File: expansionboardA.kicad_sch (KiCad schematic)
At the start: 62 parts, among them J1 DEBUG, J2 USB_A_Stacked, J3 HDMI_A, J4 FAN, P1 USB_C_Plug, U1 MAX3420EECJ, U2 GPIO_U2, U3 AMS1117-3.3, U4 GPIO_U4, U5 MCP3008T-I/SL, U6 CS4344-CZZR, U7 MAX3421EEHJ+T, Y1 Crystal, Y2 Crystal

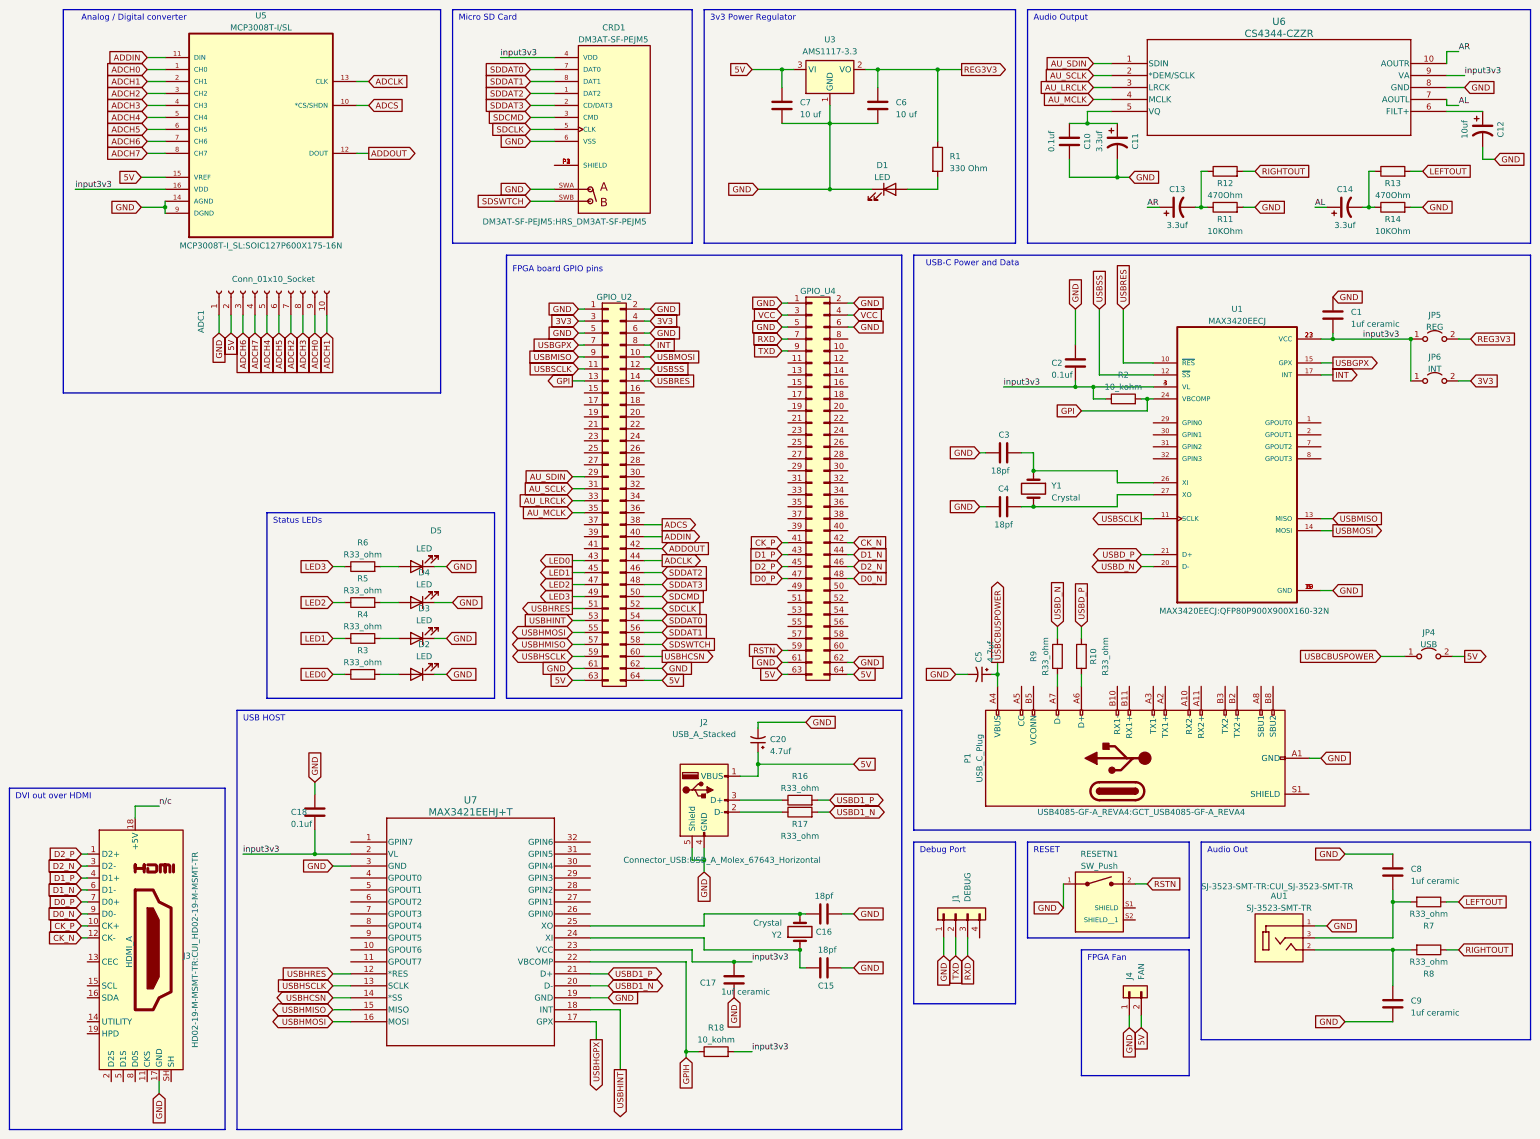
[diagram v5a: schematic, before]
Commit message: Cleaned up board layout
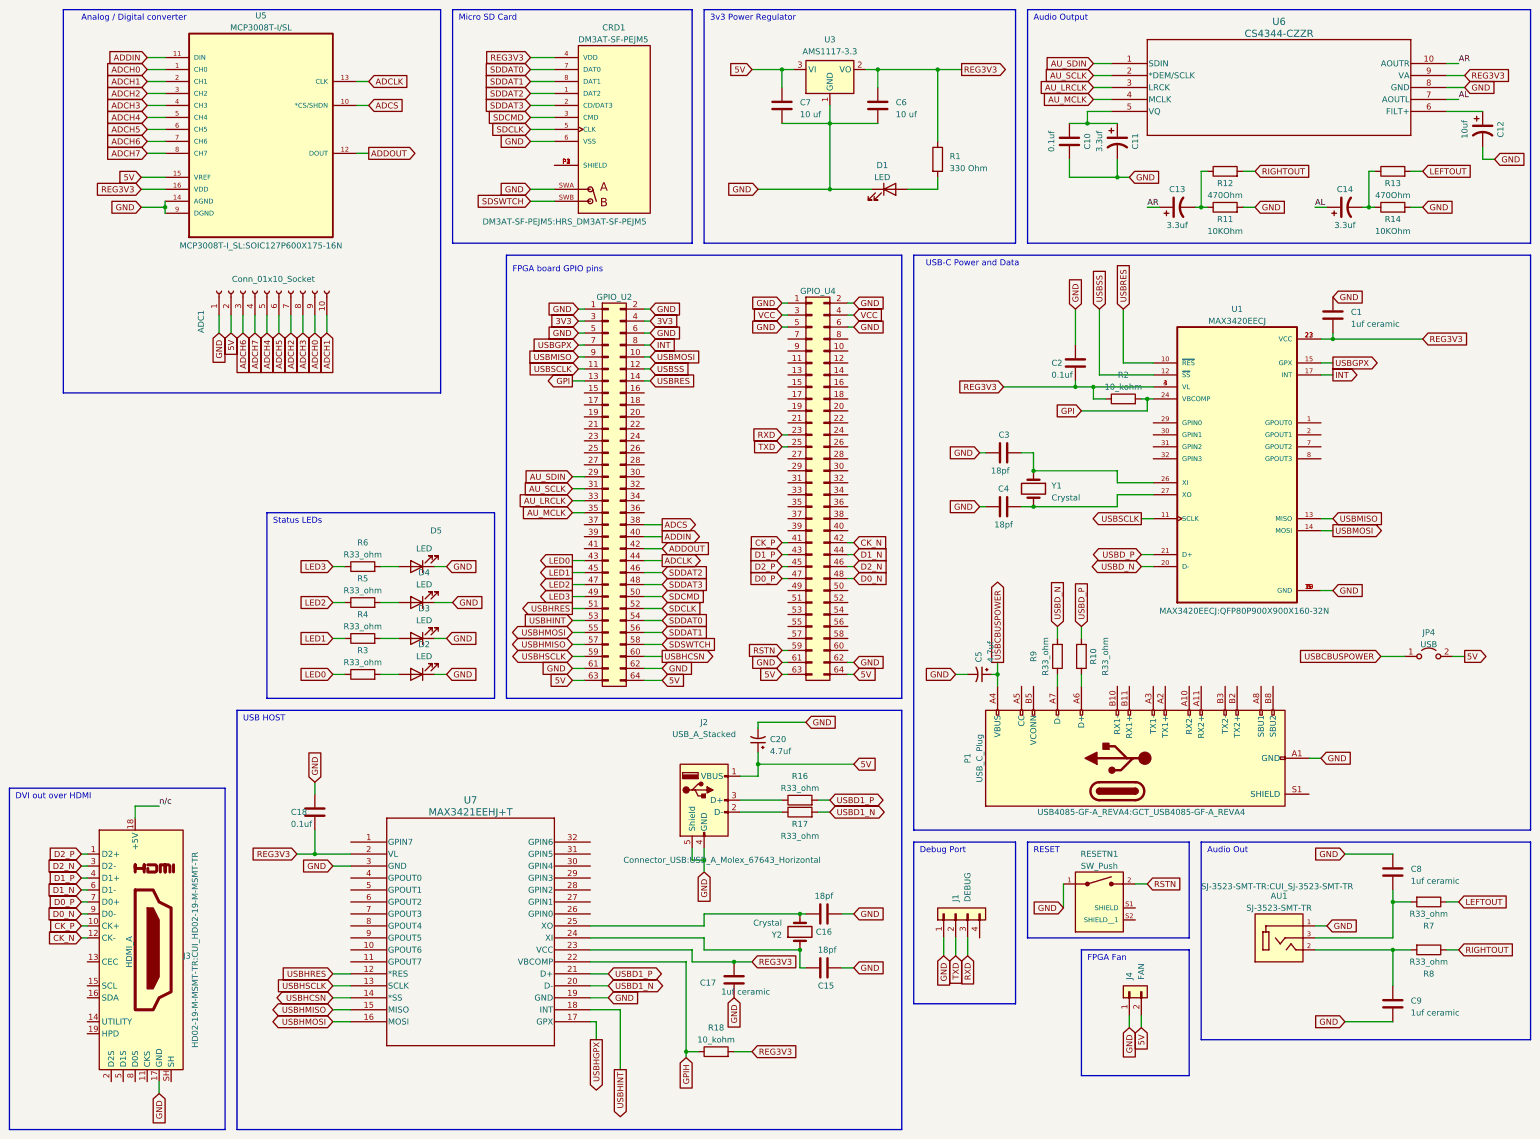
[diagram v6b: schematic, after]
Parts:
- removed JP5: REG, Jumper:SolderJumper-2_P1.3mm_Open_Pad1.0x1.5mm, symbol Jumper:Jumper_2_Open
- removed JP6: INT, Jumper:SolderJumper-2_P1.3mm_Open_Pad1.0x1.5mm, symbol Jumper:Jumper_2_Open
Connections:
- net input3v3 is gone; now on net REG3V3: C1.2, C17.2, C18.2, C2.2, CRD1.4 (VDD), R18.2, R2.1, U1.22 (VCC), U1.23 (VCC), U1.3 (VL), U1.4 (VL), U5.16 (VDD), U6.9 (VA), U7.2 (VL), U7.23 (VCC)
- net RXD: now also U4.23 (Pin_23); no longer U4.7 (Pin_7)
- net TXD: now also U4.25 (Pin_25); no longer U4.9 (Pin_9)

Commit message: Updat4ed some routing
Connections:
- net pin_removed: now reaches U4.7 (Pin_7)
- net pin_removed: now also U4.8 (Pin_8)
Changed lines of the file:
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@@
+    (stroke (width 0) (type default))
+  )
+  (wire (pts (xy 259.08 85.09) (xy 260.35 85.09))
     (stroke (width 0) (type default))
   )
@@
     (stroke (width 0) (type default))
   )
+  (wire (pts (xy 233.68 85.09) (xy 246.38 85.09))
+    (stroke (width 0) (type default))
+  )
   (wire (pts (xy 255.27 39.37) (xy 255.27 53.34))
     (stroke (width 0) (type default))
@@
     (effects (font (size 1.27 1.27)) (justify left bottom))
   )
+  (label "pin_removed" (at 233.68 85.09 0) (fields_autoplaced)
+    (effects (font (size 1.27 1.27)) (justify left bottom))
+  )
   (label "AR" (at 388.62 26.67 0) (fields_autoplaced)
     (effects (font (size 1.27 1.27)) (justify left bottom))
@@
     (effects (font (size 1.27 1.27)) (justify left bottom))
   )
+  (label "pin_removed" (at 260.35 85.09 0) (fields_autoplaced)
+    (effects (font (size 1.27 1.27)) (justify left bottom))
+  )

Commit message: Board changes
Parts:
- C20, C5: footprint Capacitor_THT:CP_Radial_D4.0mm_P1.50mm -> Capacitor_SMD:CP_Elec_4x5.4
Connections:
- net SDCMD: now also U2.54 (Pin_54); no longer U2.50 (Pin_50)
- net SDDAT0: now also U2.50 (Pin_50); no longer U2.54 (Pin_54)
- net SDDAT1: now also U2.48 (Pin_48); no longer U2.56 (Pin_56)
- net SDDAT2: now also U2.58 (Pin_58); no longer U2.46 (Pin_46)
- net SDDAT3: now also U2.56 (Pin_56); no longer U2.48 (Pin_48)
- net SDSWTCH: now also U2.46 (Pin_46); no longer U2.58 (Pin_58)
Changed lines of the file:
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@@
     (stroke (width 0) (type default))
   )
-  (wire (pts (xy 219.71 139.7) (xy 215.9 139.7))
-    (stroke (width 0) (type default))
-  )
   (wire (pts (xy 200.66 152.4) (xy 203.2 152.4))
     (stroke (width 0) (type default))
@@
     (stroke (width 0) (type default))
   )
+  (wire (pts (xy 215.9 147.32) (xy 219.71 147.32))
+    (stroke (width 0) (type default))
+  )
   (wire (pts (xy 219.71 132.08) (xy 215.9 132.08))
     (stroke (width 0) (type default))
@@
     (stroke (width 0) (type default))
   )
-  (wire (pts (xy 219.71 134.62) (xy 215.9 134.62))
-    (stroke (width 0) (type default))
-  )
   (wire (pts (xy 358.14 214.63) (xy 374.65 214.63))
     (stroke (width 0) (type default))
@@
     (stroke (width 0) (type default))
   )
-  (wire (pts (xy 219.71 144.78) (xy 215.9 144.78))
-    (stroke (width 0) (type default))
-  )
   (wire (pts (xy 388.62 214.63) (xy 386.08 214.63))
     (stroke (width 0) (type default))
@@
     (stroke (width 0) (type default))
   )
-  (wire (pts (xy 361.95 83.82) (xy 361.95 85.09))
+  (wire (pts (xy 215.9 134.62) (xy 219.71 134.62))
     (stroke (width 0) (type default))
   )
-  (wire (pts (xy 219.71 142.24) (xy 215.9 142.24))
+  (wire (pts (xy 361.95 83.82) (xy 361.95 85.09))
     (stroke (width 0) (type default))
   )
@@
     (stroke (width 0) (type default))
   )
-  (wire (pts (xy 278.13 53.34) (xy 278.13 50.8))
+  (wire (pts (xy 215.9 149.86) (xy 219.71 149.86))
     (stroke (width 0) (type default))
   )
-  (wire (pts (xy 245.11 39.37) (xy 255.27 39.37))
+  (wire (pts (xy 278.13 53.34) (xy 278.13 50.8))
     (stroke (width 0) (type default))
   )
-  (wire (pts (xy 219.71 137.16) (xy 215.9 137.16))
+  (wire (pts (xy 245.11 39.37) (xy 255.27 39.37))
     (stroke (width 0) (type default))
   )
@@
     (stroke (width 0) (type default))
   )
+  (wire (pts (xy 215.9 142.24) (xy 219.71 142.24))
+    (stroke (width 0) (type default))
+  )
   (wire (pts (xy 217.17 88.9) (xy 215.9 88.9))
     (stroke (width 0) (type default))
@@
     (stroke (width 0) (type default))
   )
-  (wire (pts (xy 219.71 149.86) (xy 215.9 149.86))
-    (stroke (width 0) (type default))
-  )
   (wire (pts (xy 364.49 194.31) (xy 374.65 194.31))
     (stroke (width 0) (type default))
@@
     (stroke (width 0) (type default))
   )
+  (wire (pts (xy 215.9 137.16) (xy 219.71 137.16))
+    (stroke (width 0) (type default))
+  )
   (wire (pts (xy 308.61 158.75) (xy 308.61 156.21))
     (stroke (width 0) (type default))
@@
     (stroke (width 0) (type default))
   )
-  (wire (pts (xy 219.71 147.32) (xy 215.9 147.32))
-    (stroke (width 0) (type default))
-  )
   (wire (pts (xy 334.01 49.53) (xy 334.01 57.15))
     (stroke (width 0) (type default))
@@
     (stroke (width 0) (type default))
   )
+  (wire (pts (xy 215.9 139.7) (xy 219.71 139.7))
+    (stroke (width 0) (type default))
+  )
   (wire (pts (xy 308.61 148.59) (xy 308.61 146.05))
     (stroke (width 0) (type default))
@@
     (stroke (width 0) (type default))
   )
+  (wire (pts (xy 215.9 144.78) (xy 219.71 144.78))
+    (stroke (width 0) (type default))
+  )
   (wire (pts (xy 149.86 224.79) (xy 153.67 224.79))
     (stroke (width 0) (type default))
@@
     )
   )
-  (global_label "SDDAT2" (shape input) (at 219.71 134.62 0) (fields_autoplaced)
+  (global_label "SDDAT2" (shape input) (at 219.71 149.86 0) (fields_autoplaced)
     (effects (font (size 1.27 1.27)) (justify left))
-    (property "Intersheetrefs" "${INTERSHEET_REFS}" (at 229.631 134.62 0)
+    (property "Intersheetrefs" "${INTERSHEET_REFS}" (at 229.631 149.86 0)
       (effects (font (size 1.27 1.27)) (justify left) hide)
     )
@@
     )
   )
-  (global_label "SDSWTCH" (shape input) (at 219.71 149.86 0) (fields_autoplaced)
+  (global_label "SDSWTCH" (shape input) (at 219.71 134.62 0) (fields_autoplaced)
     (effects (font (size 1.27 1.27)) (justify left))
-    (property "Intersheetrefs" "${INTERSHEET_REFS}" (at 231.3243 149.86 0)
+    (property "Intersheetrefs" "${INTERSHEET_REFS}" (at 231.3243 134.62 0)
       (effects (font (size 1.27 1.27)) (justify left) hide)
     )
@@
     )
   )
-  (global_label "SDCMD" (shape input) (at 219.71 139.7 0) (fields_autoplaced)
+  (global_label "SDCMD" (shape input) (at 219.71 144.78 0) (fields_autoplaced)
     (effects (font (size 1.27 1.27)) (justify left))
-    (property "Intersheetrefs" "${INTERSHEET_REFS}" (at 229.0867 139.7 0)
+    (property "Intersheetrefs" "${INTERSHEET_REFS}" (at 229.0867 144.78 0)
       (effects (font (size 1.27 1.27)) (justify left) hide)
     )
@@
     )
   )
-  (global_label "SDDAT1" (shape input) (at 219.71 147.32 0) (fields_autoplaced)
+  (global_label "SDDAT1" (shape input) (at 219.71 137.16 0) (fields_autoplaced)
     (effects (font (size 1.27 1.27)) (justify left))
-    (property "Intersheetrefs" "${INTERSHEET_REFS}" (at 229.631 147.32 0)
+    (property "Intersheetrefs" "${INTERSHEET_REFS}" (at 229.631 137.16 0)
       (effects (font (size 1.27 1.27)) (justify left) hide)
     )
@@
     )
   )
-  (global_label "SDDAT3" (shape input) (at 219.71 137.16 0) (fields_autoplaced)
+  (global_label "SDDAT3" (shape input) (at 219.71 147.32 0) (fields_autoplaced)
     (effects (font (size 1.27 1.27)) (justify left))
-    (property "Intersheetrefs" "${INTERSHEET_REFS}" (at 229.631 137.16 0)
+    (property "Intersheetrefs" "${INTERSHEET_REFS}" (at 229.631 147.32 0)
       (effects (font (size 1.27 1.27)) (justify left) hide)
     )
@@
     )
   )
-  (global_label "SDDAT0" (shape input) (at 219.71 144.78 0) (fields_autoplaced)
+  (global_label "SDDAT0" (shape input) (at 219.71 139.7 0) (fields_autoplaced)
     (effects (font (size 1.27 1.27)) (justify left))
-    (property "Intersheetrefs" "${INTERSHEET_REFS}" (at 229.631 144.78 0)
+    (property "Intersheetrefs" "${INTERSHEET_REFS}" (at 229.631 139.7 0)
       (effects (font (size 1.27 1.27)) (justify left) hide)
     )
@@
       (effects (font (size 1.27 1.27)) (justify right))
     )
-    (property "Footprint" "Capacitor_THT:CP_Radial_D4.0mm_P1.50mm" (at 287.02 156.21 0)
+    (property "Footprint" "Capacitor_SMD:CP_Elec_4x5.4" (at 287.02 156.21 0)
       (effects (font (size 1.27 1.27)) hide)
     )
@@
       (effects (font (size 1.27 1.27)) (justify right))
     )
-    (property "Footprint" "Capacitor_THT:CP_Radial_D4.0mm_P1.50mm" (at 240.03 170.18 0)
+    (property "Footprint" "Capacitor_SMD:CP_Elec_4x5.4" (at 240.03 170.18 0)
       (effects (font (size 1.27 1.27)) hide)
     )
